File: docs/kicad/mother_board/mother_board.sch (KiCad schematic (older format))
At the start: 14 parts, among them J1 EXPR, J2 TFT_CONTROL, J3 TFT_DATA, J4 SERIAL, J5 LEDS, J6 ROTARY12, J7 ROTARY34, J8 SW_OUT, J9 SW_IN, U1 myTeensy3.6

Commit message: start MAKE NEW motherboard and display_connector FOR olds TeensyExprssion box with TE2 code
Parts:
- J1: footprint 0_my_footprints:myJSTx06 -> 0_my_footprints:myPinSocket_1x06
- J4, J5: footprint 0_my_footprints:myJSTx03 -> 0_my_footprints:myPinSocket_1x03
- J6, J7, J8, J9: footprint 0_my_footprints:myJSTx05 -> 0_my_footprints:myPinSocket_1x05
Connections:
- net +3V3: now also J1.5 (Pin_5), J2.7 (Pin_7), J7.5 (Pin_5); no longer J1.2 (Pin_2), J2.2 (Pin_2), J7.1 (Pin_1)
- net +5V: now also J2.8 (Pin_8); no longer J2.1 (Pin_1)
- net EXPR1: now also J1.4 (Pin_4); no longer J1.3 (Pin_3)
- net EXPR2: now also J1.3 (Pin_3); no longer J1.4 (Pin_4)
- net EXPR3: now also J1.2 (Pin_2); no longer J1.5 (Pin_5)
- net EXPR4: now also J1.1 (Pin_1); no longer J1.6 (Pin_6)
- net GND: now also J1.6 (Pin_6), J2.1 (Pin_1), J6.5 (Pin_5); no longer J1.1 (Pin_1), J2.8 (Pin_8), J6.1 (Pin_1)
- net ROT1A: now also J6.1 (Pin_1); no longer J6.5 (Pin_5)
- net ROT1B: now also J6.2 (Pin_2); no longer J6.4 (Pin_4)
- net ROT2A: now also J6.3 (Pin_3), U1.6 (4); no longer J6.2 (Pin_2), U1.8 (6)
- net ROT2B: now also J6.4 (Pin_4), U1.8 (6); no longer J6.3 (Pin_3), U1.6 (4)
- net ROT3A: now also J7.1 (Pin_1); no longer J7.5 (Pin_5)
- net ROT3B: now also J7.2 (Pin_2); no longer J7.4 (Pin_4)
- net ROT4A: now also J7.3 (Pin_3), U1.13 (11); no longer J7.2 (Pin_2), U1.14 (12)
- net ROT4B: now also J7.4 (Pin_4), U1.14 (12); no longer J7.3 (Pin_3), U1.13 (11)
- net SW_IN1: now also J9.2 (Pin_2), U1.22 (30); no longer J9.5 (Pin_5), U1.21 (29)
- net SW_IN2: now also J9.3 (Pin_3), U1.23 (31); no longer J9.4 (Pin_4), U1.22 (30)
- net SW_IN3: now also J9.4 (Pin_4), U1.24 (32); no longer J9.3 (Pin_3), U1.23 (31)
- net SW_IN4: now also J9.5 (Pin_5), U1.25 (33_(A14)); no longer J9.2 (Pin_2), U1.24 (32)
- net SW_OUT1: now also J8.2 (Pin_2), U1.17 (25); no longer J8.5 (Pin_5), U1.16 (24)
- net SW_OUT2: now also J8.3 (Pin_3), U1.18 (26); no longer J8.4 (Pin_4), U1.17 (25)
- net SW_OUT3: now also J8.4 (Pin_4), U1.19 (27); no longer J8.3 (Pin_3), U1.18 (26)
- net SW_OUT4: now also J8.5 (Pin_5), U1.20 (28); no longer J8.2 (Pin_2), U1.19 (27)
- net TFT_CD_RS: now also J2.4 (Pin_4); no longer J2.5 (Pin_5)
- net TFT_CS: now also J2.5 (Pin_5); no longer J2.4 (Pin_4)
- net TFT_DAT0: now also J3.7 (Pin_7); no longer J3.2 (Pin_2)
- net TFT_DAT1: now also J3.8 (Pin_8); no longer J3.1 (Pin_1)
- net TFT_DAT2: now also J3.1 (Pin_1); no longer J3.8 (Pin_8)
- net TFT_DAT3: now also J3.2 (Pin_2); no longer J3.7 (Pin_7)
- net TFT_DAT4: now also J3.3 (Pin_3); no longer J3.6 (Pin_6)
- net TFT_DAT5: now also J3.4 (Pin_4); no longer J3.5 (Pin_5)
- net TFT_DAT6: now also J3.5 (Pin_5); no longer J3.4 (Pin_4)
- net TFT_DAT7: now also J3.6 (Pin_6); no longer J3.3 (Pin_3)
- net TFT_RD: now also J2.2 (Pin_2); no longer J2.7 (Pin_7)
- net TFT_RES: now also J2.6 (Pin_6); no longer J2.3 (Pin_3)
- net TFT_WR: now also J2.3 (Pin_3); no longer J2.6 (Pin_6)
- net SW_IN5 renamed SW_IN0
- net SW_IN0: now also U1.21 (29); no longer U1.25 (33_(A14))
- net SW_OUT5 renamed SW_OUT0
- net SW_OUT0: now also U1.16 (24); no longer U1.20 (28)
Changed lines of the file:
@@
 F 0 "J5" V 4250 5700 50  0000 L CNN
 F 1 "LEDS" V 4150 5650 50  0000 L CNN
-F 2 "0_my_footprints:myJSTx03" H 4000 5750 50  0001 C CNN
+F 2 "0_my_footprints:myPinSocket_1x03" H 4000 5750 50  0001 C CNN
 F 3 "~" H 4000 5750 50  0001 C CNN
 	1    4000 5750
@@
 F 0 "J6" V 4950 5700 50  0000 L CNN
 F 1 "ROTARY12" V 4850 5550 50  0000 L CNN
-F 2 "0_my_footprints:myJSTx05" H 4700 5750 50  0001 C CNN
+F 2 "0_my_footprints:myPinSocket_1x05" H 4700 5750 50  0001 C CNN
 F 3 "~" H 4700 5750 50  0001 C CNN
 	1    4700 5750
@@
 F 0 "J1" V 4200 1300 50  0000 R CNN
 F 1 "EXPR" V 4100 1350 50  0000 R CNN
-F 2 "0_my_footprints:myJSTx06" H 3950 1300 50  0001 C CNN
+F 2 "0_my_footprints:myPinSocket_1x06" H 3950 1300 50  0001 C CNN
 F 3 "~" H 3950 1300 50  0001 C CNN
 	1    3950 1300
@@
 F 0 "J7" V 5550 5700 50  0000 L CNN
 F 1 "ROTARY34" V 5450 5550 50  0000 L CNN
-F 2 "0_my_footprints:myJSTx05" H 5300 5750 50  0001 C CNN
+F 2 "0_my_footprints:myPinSocket_1x05" H 5300 5750 50  0001 C CNN
 F 3 "~" H 5300 5750 50  0001 C CNN
 	1    5300 5750
@@
 F 0 "J8" V 6200 5700 50  0000 L CNN
 F 1 "SW_OUT" V 6100 5650 50  0000 L CNN
-F 2 "0_my_footprints:myJSTx05" H 5950 5750 50  0001 C CNN
+F 2 "0_my_footprints:myPinSocket_1x05" H 5950 5750 50  0001 C CNN
 F 3 "~" H 5950 5750 50  0001 C CNN
 	1    5950 5750
@@
 F 0 "J9" V 6700 5700 50  0000 L CNN
 F 1 "SW_IN" V 6600 5650 50  0000 L CNN
-F 2 "0_my_footprints:myJSTx05" H 6450 5750 50  0001 C CNN
+F 2 "0_my_footprints:myPinSocket_1x05" H 6450 5750 50  0001 C CNN
 F 3 "~" H 6450 5750 50  0001 C CNN
 	1    6450 5750
@@
 F 0 "J4" V 4900 6100 50  0000 L CNN
 F 1 "SERIAL" V 5000 6050 50  0000 L CNN
-F 2 "0_my_footprints:myJSTx03" H 5000 6650 50  0001 C CNN
+F 2 "0_my_footprints:myPinSocket_1x03" H 5000 6650 50  0001 C CNN
 F 3 "~" H 5000 6650 50  0001 C CNN
 	1    5000 6650
@@
 L power:+3V3 #PWR016
 U 1 1 64C9FDB5
-P 5500 5550
-F 0 "#PWR016" H 5500 5400 50  0001 C CNN
-F 1 "+3V3" V 5500 5750 50  0000 C CNN
-F 2 "" H 5500 5550 50  0001 C CNN
-F 3 "" H 5500 5550 50  0001 C CNN
-	1    5500 5550
+P 5100 5550
+F 0 "#PWR016" H 5100 5400 50  0001 C CNN
+F 1 "+3V3" V 5100 5750 50  0000 C CNN
+F 2 "" H 5100 5550 50  0001 C CNN
+F 3 "" H 5100 5550 50  0001 C CNN
+	1    5100 5550
 	1    0    0    -1
 $EndComp
@@
 L power:GND #PWR015
 U 1 1 64CA12B5
-P 4900 5550
-F 0 "#PWR015" H 4900 5300 50  0001 C CNN
-F 1 "GND" V 4900 5350 50  0000 C CNN
-F 2 "" H 4900 5550 50  0001 C CNN
-F 3 "" H 4900 5550 50  0001 C CNN
-	1    4900 5550
+P 4500 5550
+F 0 "#PWR015" H 4500 5300 50  0001 C CNN
+F 1 "GND" V 4500 5350 50  0000 C CNN
+F 2 "" H 4500 5550 50  0001 C CNN
+F 3 "" H 4500 5550 50  0001 C CNN
+	1    4500 5550
 	-1   0    0    1
 $EndComp
@@
 	-1   0    0    1
 $EndComp
-Text GLabel 4950 4250 3    50   Input ~ 0
-LEDS
 Text GLabel 4650 4250 3    50   Input ~ 0
 ROT1A
@@
 ROT1B
 Text GLabel 4850 4250 3    50   Input ~ 0
-ROT2B
-Text GLabel 5050 4250 3    50   Input ~ 0
 ROT2A
 Text GLabel 5150 4250 3    50   Input ~ 0
@@
 Text GLabel 5450 4250 3    50   Input ~ 0
 ROT3B
+Text GLabel 5650 4250 3    50   Input ~ 0
+ROT4B
 Text GLabel 5550 4250 3    50   Input ~ 0
+ROT4A
+Text GLabel 4900 5550 1    50   Input ~ 0
+ROT1A
+Text GLabel 4800 5550 1    50   Input ~ 0
+ROT1B
+Text GLabel 4600 5550 1    50   Input ~ 0
+ROT2B
+Text GLabel 4700 5550 1    50   Input ~ 0
+ROT2A
+Text GLabel 5500 5550 1    50   Input ~ 0
+ROT3A
+Text GLabel 5400 5550 1    50   Input ~ 0
+ROT3B
+Text GLabel 5200 5550 1    50   Input ~ 0
 ROT4B
-Text GLabel 5650 4250 3    50   Input ~ 0
-ROT4A
-Text GLabel 4500 5550 1    50   Input ~ 0
-ROT1A
-Text GLabel 4600 5550 1    50   Input ~ 0
-ROT1B
-Text GLabel 4700 5550 1    50   Input ~ 0
-ROT2B
-Text GLabel 4800 5550 1    50   Input ~ 0
-ROT2A
-Text GLabel 5100 5550 1    50   Input ~ 0
-ROT3A
-Text GLabel 5200 5550 1    50   Input ~ 0
-ROT3B
 Text GLabel 5300 5550 1    50   Input ~ 0
-ROT4B
-Text GLabel 5400 5550 1    50   Input ~ 0
 ROT4A
 Text GLabel 5850 4250 3    50   Input ~ 0
+SW_OUT0
+Text GLabel 5950 4250 3    50   Input ~ 0
 SW_OUT1
-Text GLabel 5950 4250 3    50   Input ~ 0
+Text GLabel 6050 4250 3    50   Input ~ 0
 SW_OUT2
-Text GLabel 6050 4250 3    50   Input ~ 0
+Text GLabel 6150 4250 3    50   Input ~ 0
 SW_OUT3
-Text GLabel 6150 4250 3    50   Input ~ 0
+Text GLabel 6250 4250 3    50   Input ~ 0
 SW_OUT4
-Text GLabel 6250 4250 3    50   Input ~ 0
-SW_OUT5
 Text GLabel 6350 4250 3    50   Input ~ 0
+SW_IN0
+Text GLabel 6450 4250 3    50   Input ~ 0
 SW_IN1
-Text GLabel 6450 4250 3    50   Input ~ 0
+Text GLabel 6550 4250 3    50   Input ~ 0
 SW_IN2
-Text GLabel 6550 4250 3    50   Input ~ 0
+Text GLabel 6650 4250 3    50   Input ~ 0
 SW_IN3
-Text GLabel 6650 4250 3    50   Input ~ 0
+Text GLabel 6650 2700 1    50   Input ~ 0
 SW_IN4
-Text GLabel 6650 2700 1    50   Input ~ 0
-SW_IN5
+Text GLabel 6050 5550 1    50   Input ~ 0
+SW_OUT1
+Text GLabel 5950 5550 1    50   Input ~ 0
+SW_OUT2
+Text GLabel 5850 5550 1    50   Input ~ 0
+SW_OUT3
 Text GLabel 5750 5550 1    50   Input ~ 0
-SW_OUT1
-Text GLabel 5850 5550 1    50   Input ~ 0
-SW_OUT2
-Text GLabel 5950 5550 1    50   Input ~ 0
-SW_OUT3
-Text GLabel 6050 5550 1    50   Input ~ 0
 SW_OUT4
 Text GLabel 6150 5550 1    50   Input ~ 0
-SW_OUT5
+SW_OUT0
+Text GLabel 6550 5550 1    50   Input ~ 0
+SW_IN1
+Text GLabel 6450 5550 1    50   Input ~ 0
+SW_IN2
+Text GLabel 6350 5550 1    50   Input ~ 0
+SW_IN3
 Text GLabel 6250 5550 1    50   Input ~ 0
-SW_IN1
-Text GLabel 6350 5550 1    50   Input ~ 0
-SW_IN2
-Text GLabel 6450 5550 1    50   Input ~ 0
-SW_IN3
-Text GLabel 6550 5550 1    50   Input ~ 0
 SW_IN4
 Text GLabel 6650 5550 1    50   Input ~ 0
-SW_IN5
+SW_IN0
 $Comp
 L power:GND #PWR01
 U 1 1 64CFCC09
-P 3750 1500
-F 0 "#PWR01" H 3750 1250 50  0001 C CNN
-F 1 "GND" V 3750 1300 50  0000 C CNN
-F 2 "" H 3750 1500 50  0001 C CNN
-F 3 "" H 3750 1500 50  0001 C CNN
-	1    3750 1500
-	1    0    0    -1
+P 4250 1500
+F 0 "#PWR01" H 4250 1250 50  0001 C CNN
+F 1 "GND" V 4250 1300 50  0000 C CNN
+F 2 "" H 4250 1500 50  0001 C CNN
+F 3 "" H 4250 1500 50  0001 C CNN
+	1    4250 1500
+	-1   0    0    -1
 $EndComp
 $Comp
@@
 	1    0    0    -1
 $EndComp
+Text GLabel 4050 1500 3    50   Input ~ 0
+EXPR1
 Text GLabel 3950 1500 3    50   Input ~ 0
-EXPR1
-Text GLabel 4050 1500 3    50   Input ~ 0
 EXPR2
-Text GLabel 4150 1500 3    50   Input ~ 0
+Text GLabel 3850 1500 3    50   Input ~ 0
 EXPR3
-Text GLabel 4250 1500 3    50   Input ~ 0
+Text GLabel 3750 1500 3    50   Input ~ 0
 EXPR4
 Text GLabel 4650 2700 1    50   Input ~ 0
@@
 L power:+5V #PWR02
 U 1 1 64D14F5D
+P 5350 1500
+F 0 "#PWR02" H 5350 1350 50  0001 C CNN
+F 1 "+5V" V 5350 1700 50  0000 C CNN
+F 2 "" H 5350 1500 50  0001 C CNN
+F 3 "" H 5350 1500 50  0001 C CNN
+	1    5350 1500
+	1    0    0    1
+$EndComp
+$Comp
+L power:GND #PWR04
+U 1 1 64D19F15
 P 4650 1500
-F 0 "#PWR02" H 4650 1350 50  0001 C CNN
-F 1 "+5V" V 4650 1700 50  0000 C CNN
+F 0 "#PWR04" H 4650 1250 50  0001 C CNN
+F 1 "GND" V 4650 1300 50  0000 C CNN
 F 2 "" H 4650 1500 50  0001 C CNN
 F 3 "" H 4650 1500 50  0001 C CNN
 	1    4650 1500
-	-1   0    0    1
-$EndComp
-$Comp
-L power:GND #PWR04
-U 1 1 64D19F15
-P 5350 1500
-F 0 "#PWR04" H 5350 1250 50  0001 C CNN
-F 1 "GND" V 5350 1300 50  0000 C CNN
-F 2 "" H 5350 1500 50  0001 C CNN
-F 3 "" H 5350 1500 50  0001 C CNN
-	1    5350 1500
-	1    0    0    -1
-$EndComp
+	-1   0    0    -1
+$EndComp
+Text GLabel 5150 1500 3    50   Input ~ 0
+TFT_RES
+Text GLabel 5050 1500 3    50   Input ~ 0
+TFT_CS
+Text GLabel 4950 1500 3    50   Input ~ 0
+TFT_CD_RS
 Text GLabel 4850 1500 3    50   Input ~ 0
-TFT_RES
-Text GLabel 4950 1500 3    50   Input ~ 0
-TFT_CS
-Text GLabel 5050 1500 3    50   Input ~ 0
-TFT_CD_RS
-Text GLabel 5150 1500 3    50   Input ~ 0
 TFT_WR
-Text GLabel 5250 1500 3    50   Input ~ 0
+Text GLabel 4750 1500 3    50   Input ~ 0
 TFT_RD
+Text GLabel 6300 1500 3    50   Input ~ 0
+TFT_DAT1
+Text GLabel 6200 1500 3    50   Input ~ 0
+TFT_DAT0
+Text GLabel 6100 1500 3    50   Input ~ 0
+TFT_DAT7
+Text GLabel 6000 1500 3    50   Input ~ 0
+TFT_DAT6
+Text GLabel 5900 1500 3    50   Input ~ 0
+TFT_DAT5
+Text GLabel 5800 1500 3    50   Input ~ 0
+TFT_DAT4
+Text GLabel 5700 1500 3    50   Input ~ 0
+TFT_DAT3
 Text GLabel 5600 1500 3    50   Input ~ 0
-TFT_DAT1
-Text GLabel 5700 1500 3    50   Input ~ 0
-TFT_DAT0
-Text GLabel 5800 1500 3    50   Input ~ 0
-TFT_DAT7
-Text GLabel 5900 1500 3    50   Input ~ 0
-TFT_DAT6
-Text GLabel 6000 1500 3    50   Input ~ 0
-TFT_DAT5
-Text GLabel 6100 1500 3    50   Input ~ 0
-TFT_DAT4
-Text GLabel 6200 1500 3    50   Input ~ 0
-TFT_DAT3
-Text GLabel 6300 1500 3    50   Input ~ 0
 TFT_DAT2
 Text GLabel 5150 2700 1    50   Input ~ 0
@@
 L power:+3V3 #PWR03
 U 1 1 64D171C2
-P 4750 1500
-F 0 "#PWR03" H 4750 1350 50  0001 C CNN
-F 1 "+3V3" V 4750 1700 50  0000 C CNN
-F 2 "" H 4750 1500 50  0001 C CNN
-F 3 "" H 4750 1500 50  0001 C CNN
-	1    4750 1500
-	-1   0    0    1
+P 5250 1500
+F 0 "#PWR03" H 5250 1350 50  0001 C CNN
+F 1 "+3V3" V 5250 1700 50  0000 C CNN
+F 2 "" H 5250 1500 50  0001 C CNN
+F 3 "" H 5250 1500 50  0001 C CNN
+	1    5250 1500
+	1    0    0    1
 $EndComp
 $Comp
 L power:+3V3 #PWR06
 U 1 1 64D07CE1
-P 3850 1500
-F 0 "#PWR06" H 3850 1350 50  0001 C CNN
-F 1 "+3V3" V 3850 1700 50  0000 C CNN
-F 2 "" H 3850 1500 50  0001 C CNN
-F 3 "" H 3850 1500 50  0001 C CNN
-	1    3850 1500
-	-1   0    0    1
+P 4150 1500
+F 0 "#PWR06" H 4150 1350 50  0001 C CNN
+F 1 "+3V3" V 4150 1700 50  0000 C CNN
+F 2 "" H 4150 1500 50  0001 C CNN
+F 3 "" H 4150 1500 50  0001 C CNN
+	1    4150 1500
+	1    0    0    1
 $EndComp
 Text GLabel 3000 1800 1    50   Input ~ 0
@@
 	1    0    0    -1
 $EndComp
+Text GLabel 5050 4250 3    50   Input ~ 0
+ROT2B
+Text GLabel 4950 4250 3    50   Input ~ 0
+LEDS
 $EndSCHEMATC

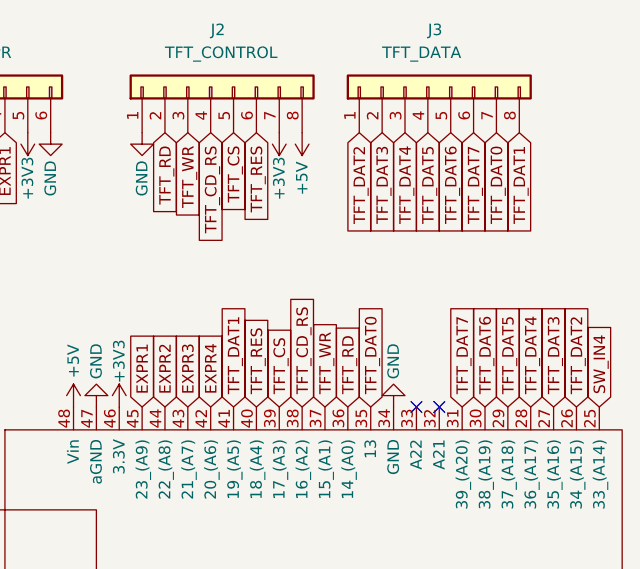
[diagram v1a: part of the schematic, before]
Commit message: kicad - corrected TFT data pin order for new teensyExpression2 board/code
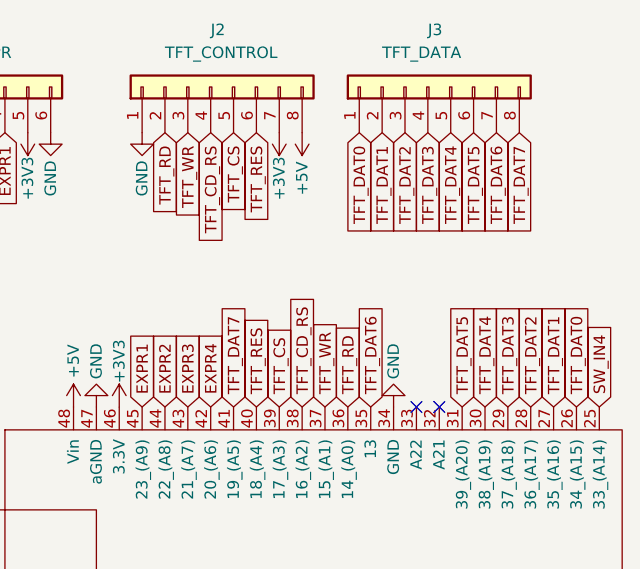
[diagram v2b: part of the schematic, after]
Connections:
- net TFT_DAT0: now also J3.1 (Pin_1), U1.26 (34_(A15)); no longer J3.7 (Pin_7), U1.35 (13)
- net TFT_DAT1: now also J3.2 (Pin_2), U1.27 (35_(A16)); no longer J3.8 (Pin_8), U1.41 (19_(A5))
- net TFT_DAT2: now also J3.3 (Pin_3), U1.28 (36_(A17)); no longer J3.1 (Pin_1), U1.26 (34_(A15))
- net TFT_DAT3: now also J3.4 (Pin_4), U1.29 (37_(A18)); no longer J3.2 (Pin_2), U1.27 (35_(A16))
- net TFT_DAT4: now also J3.5 (Pin_5), U1.30 (38_(A19)); no longer J3.3 (Pin_3), U1.28 (36_(A17))
- net TFT_DAT5: now also J3.6 (Pin_6), U1.31 (39_(A20)); no longer J3.4 (Pin_4), U1.29 (37_(A18))
- net TFT_DAT6: now also J3.7 (Pin_7), U1.35 (13); no longer J3.5 (Pin_5), U1.30 (38_(A19))
- net TFT_DAT7: now also J3.8 (Pin_8), U1.41 (19_(A5)); no longer J3.6 (Pin_6), U1.31 (39_(A20))
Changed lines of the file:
@@
 Text GLabel 4750 1500 3    50   Input ~ 0
 TFT_RD
+Text GLabel 5700 1500 3    50   Input ~ 0
+TFT_DAT1
+Text GLabel 5600 1500 3    50   Input ~ 0
+TFT_DAT0
 Text GLabel 6300 1500 3    50   Input ~ 0
-TFT_DAT1
+TFT_DAT7
 Text GLabel 6200 1500 3    50   Input ~ 0
-TFT_DAT0
+TFT_DAT6
 Text GLabel 6100 1500 3    50   Input ~ 0
-TFT_DAT7
+TFT_DAT5
 Text GLabel 6000 1500 3    50   Input ~ 0
-TFT_DAT6
+TFT_DAT4
 Text GLabel 5900 1500 3    50   Input ~ 0
-TFT_DAT5
+TFT_DAT3
 Text GLabel 5800 1500 3    50   Input ~ 0
-TFT_DAT4
-Text GLabel 5700 1500 3    50   Input ~ 0
-TFT_DAT3
-Text GLabel 5600 1500 3    50   Input ~ 0
 TFT_DAT2
 Text GLabel 5150 2700 1    50   Input ~ 0
@@
 Text GLabel 5550 2700 1    50   Input ~ 0
 TFT_RD
+Text GLabel 6450 2700 1    50   Input ~ 0
+TFT_DAT1
+Text GLabel 6550 2700 1    50   Input ~ 0
+TFT_DAT0
 Text GLabel 5050 2700 1    50   Input ~ 0
-TFT_DAT1
+TFT_DAT7
 Text GLabel 5650 2700 1    50   Input ~ 0
-TFT_DAT0
+TFT_DAT6
 Text GLabel 6050 2700 1    50   Input ~ 0
-TFT_DAT7
+TFT_DAT5
 Text GLabel 6150 2700 1    50   Input ~ 0
-TFT_DAT6
+TFT_DAT4
 Text GLabel 6250 2700 1    50   Input ~ 0
-TFT_DAT5
+TFT_DAT3
 Text GLabel 6350 2700 1    50   Input ~ 0
-TFT_DAT4
-Text GLabel 6450 2700 1    50   Input ~ 0
-TFT_DAT3
-Text GLabel 6550 2700 1    50   Input ~ 0
 TFT_DAT2
 NoConn ~ 5850 2700

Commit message: AFTER BUILD NEW PCBs - corrected display connector pins; removed old combined plot and gcode file
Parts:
- R1, R2, R3, R4: value 10K -> 47K
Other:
- note added: "Pulldown resistors\nare optional"
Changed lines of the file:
@@
 P 3100 1950
 F 0 "R2" V 3100 1400 50  0000 L CNN
-F 1 "10K" V 3100 1950 50  0000 C CNN
+F 1 "47K" V 3100 1950 50  0000 C CNN
 F 2 "0_my_footprints:myResistor" V 3030 1950 50  0001 C CNN
 F 3 "~" H 3100 1950 50  0001 C CNN
@@
 P 3200 1950
 F 0 "R3" V 3200 1400 50  0000 L CNN
-F 1 "10K" V 3200 1950 50  0000 C CNN
+F 1 "47K" V 3200 1950 50  0000 C CNN
 F 2 "0_my_footprints:myResistor" V 3130 1950 50  0001 C CNN
 F 3 "~" H 3200 1950 50  0001 C CNN
@@
 P 3300 1950
 F 0 "R4" V 3300 1400 50  0000 L CNN
-F 1 "10K" V 3300 1950 50  0000 C CNN
+F 1 "47K" V 3300 1950 50  0000 C CNN
 F 2 "0_my_footprints:myResistor" V 3230 1950 50  0001 C CNN
 F 3 "~" H 3300 1950 50  0001 C CNN
@@
 P 3000 1950
 F 0 "R1" V 3000 1400 50  0000 L CNN
-F 1 "10K" V 3000 1950 50  0000 C CNN
+F 1 "47K" V 3000 1950 50  0000 C CNN
 F 2 "0_my_footprints:myResistor" V 2930 1950 50  0001 C CNN
 F 3 "~" H 3000 1950 50  0001 C CNN
@@
 Text GLabel 4950 4250 3    50   Input ~ 0
 LEDS
+Text Notes 2150 2000 0    50   ~ 0
+Pulldown resistors\nare optional
 $EndSCHEMATC

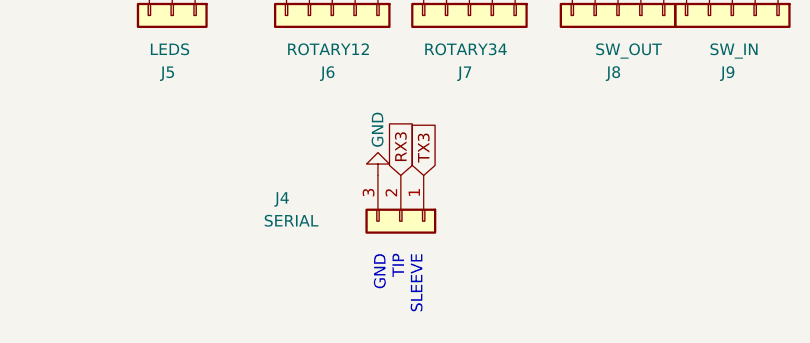
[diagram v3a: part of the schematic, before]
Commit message: AFTER TE2 REBUILD - new gcode for left, top, and back.  Corrected symbols for Serial Connector (and on motherboard)
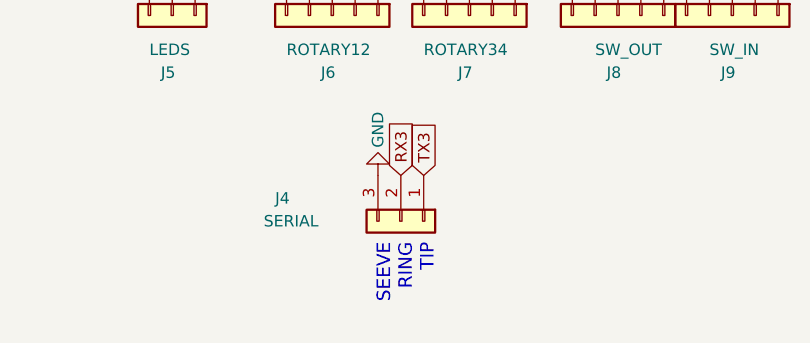
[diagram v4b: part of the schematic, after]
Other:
- note added: "SEEVE\nRING\nTIP"
- note removed: "GND\nTIP\nSLEEVE"
